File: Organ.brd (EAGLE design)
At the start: 55.5 x 26.7 mm, 16 parts, among them IC1 NE555

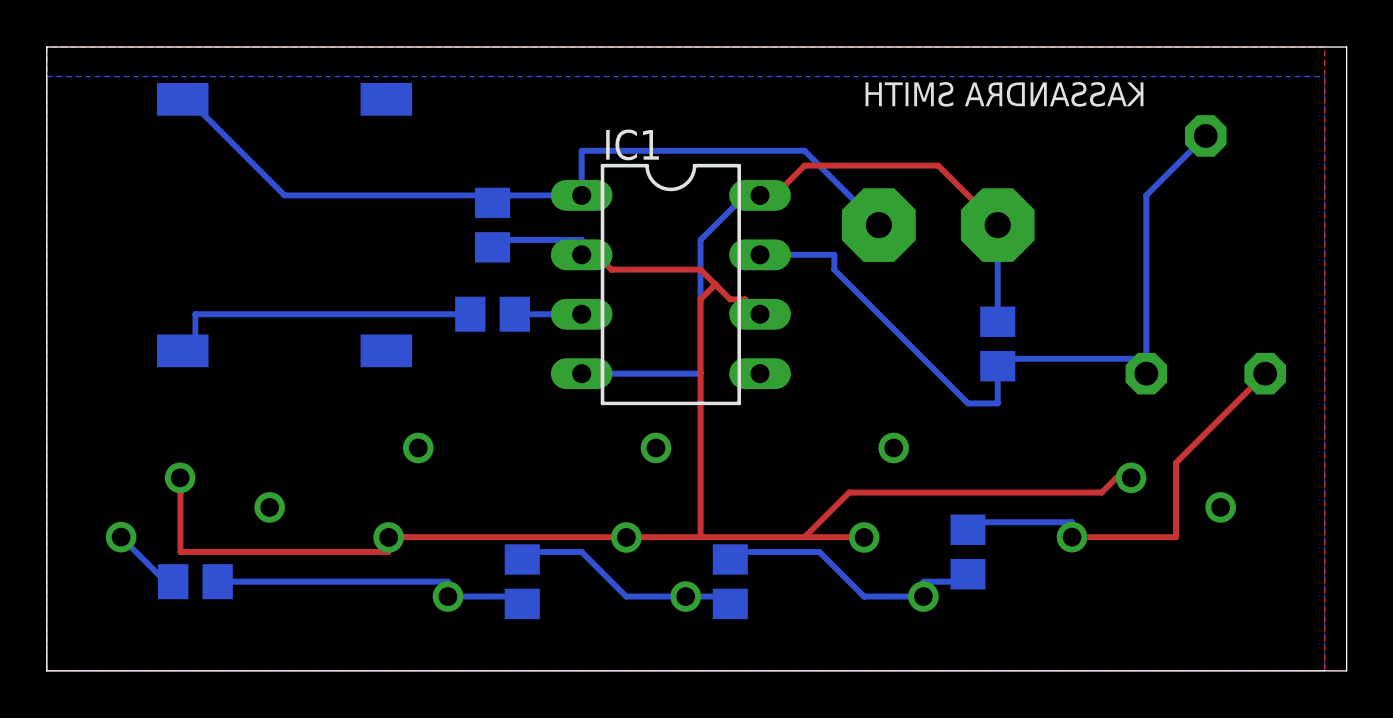
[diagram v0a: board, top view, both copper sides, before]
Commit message: Use new sizing standards
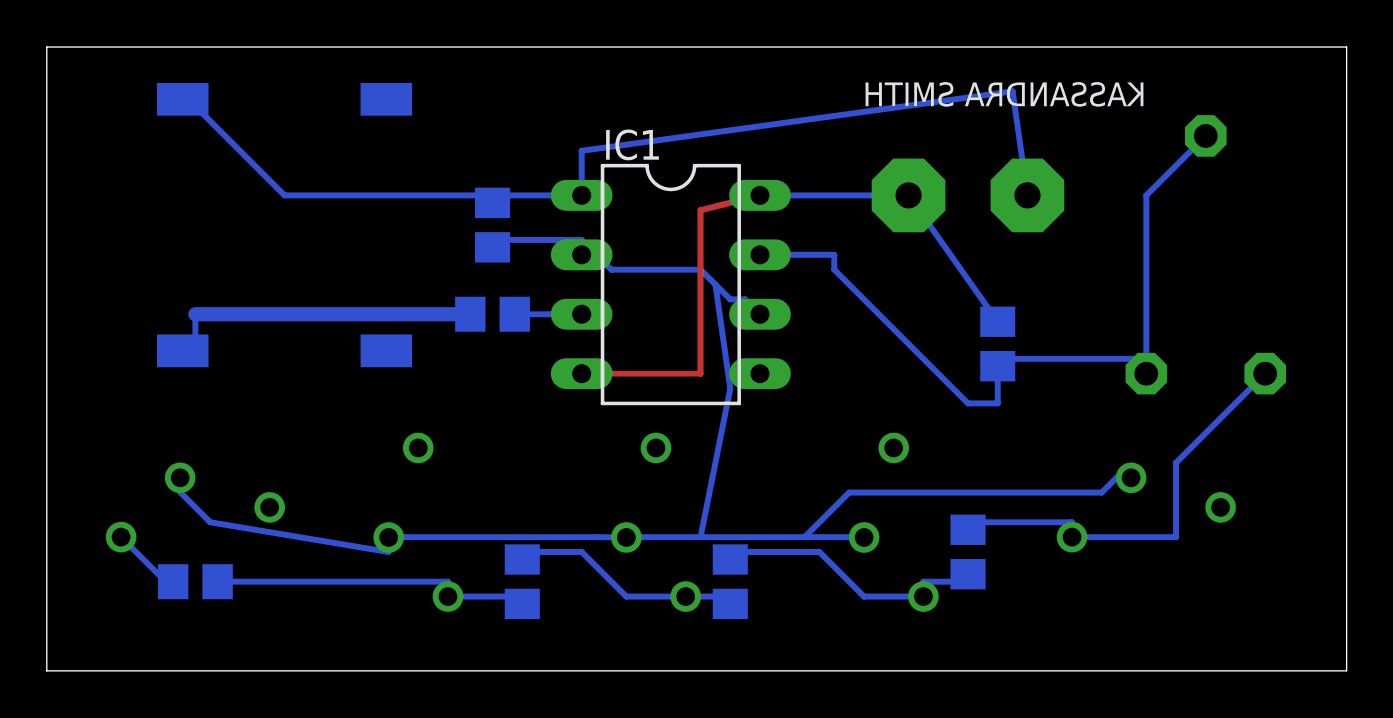
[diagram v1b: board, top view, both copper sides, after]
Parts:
- moved G1 1.80 mm to (39.4, 64.8), turned to 270 degrees
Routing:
- net GROUND: track 34.9 -> 44.0 mm
- net VCC: track 30.0 -> 27.6 mm
- net DISCHARGE: track 72.5 -> 70.5 mm
- removed copper zone on layer 1, net GND
- removed copper zone on layer 16, net GND
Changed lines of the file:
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@@
 <setting verticaltext="up"/>
 </settings>
-<grid distance="0.05" unitdist="inch" unit="inch" style="lines" multiple="1" display="no" altdistance="0.025" altunitdist="inch" altunit="inch"/>
+<grid distance="0.05" unitdist="inch" unit="mm" style="lines" multiple="1" display="no" altdistance="0.025" altunitdist="inch" altunit="mm"/>
 <layers>
 <layer number="1" name="Top" color="4" fill="1" visible="yes" active="yes"/>
@@
 <element name="C1" library="rcl" package="C0805" value="100uF" x="19.05" y="59.69" rot="MR0"/>
 <element name="C2" library="rcl" package="C0805" value="100nF" x="19.05" y="63.5" rot="MR90"/>
-<element name="G1" library="battery" package="AB9V" value="AB9V" x="38.1" y="63.5" rot="MR90"/>
+<element name="G1" library="battery" package="AB9V" value="AB9V" x="39.37" y="64.77" rot="MR270"/>
 <element name="IC1" library="st-microelectronics" package="DIL-08" value="NE555" x="26.67" y="60.96" rot="R270">
 <attribute name="OC_NEWARK" value="89K1486" x="26.67" y="60.96" size="1.778" layer="27" rot="R270" display="off"/>
@@
 <contactref element="R1" pad="2"/>
 <contactref element="IC1" pad="8"/>
-<wire x1="40.64" y1="63.5" x2="40.64" y2="59.37" width="0.254" layer="16"/>
-<wire x1="27.94" y1="57.15" x2="22.86" y2="57.15" width="0.254" layer="16"/>
-<wire x1="27.94" y1="62.865" x2="27.94" y2="57.15" width="0.254" layer="16"/>
-<wire x1="29.845" y1="64.77" x2="27.94" y2="62.865" width="0.254" layer="16"/>
-<wire x1="30.48" y1="64.77" x2="29.845" y2="64.77" width="0.254" layer="16"/>
-<wire x1="38.1" y1="66.04" x2="40.64" y2="63.5" width="0.254" layer="1"/>
-<wire x1="32.385" y1="66.04" x2="38.1" y2="66.04" width="0.254" layer="1"/>
-<wire x1="31.115" y1="64.77" x2="32.385" y2="66.04" width="0.254" layer="1"/>
-<wire x1="30.48" y1="64.77" x2="31.115" y2="64.77" width="0.254" layer="1"/>
+<wire x1="36.83" y1="64.77" x2="40.64" y2="59.37" width="0.254" layer="16"/>
+<wire x1="27.94" y1="57.15" x2="22.86" y2="57.15" width="0.254" layer="1"/>
+<wire x1="27.94" y1="64.135" x2="27.94" y2="57.15" width="0.254" layer="1"/>
+<wire x1="30.48" y1="64.77" x2="27.94" y2="64.135" width="0.254" layer="1"/>
+<wire x1="30.48" y1="64.77" x2="36.83" y2="64.77" width="0.254" layer="16"/>
 </signal>
 <signal name="POT">
@@
 <wire x1="43.815" y1="50.165" x2="43.815" y2="50.8" width="0.254" layer="16"/>
 <wire x1="39.37" y1="50.8" x2="39.37" y2="50.48" width="0.254" layer="16"/>
-<wire x1="48.26" y1="53.34" x2="52.07" y2="57.15" width="0.254" layer="1"/>
-<wire x1="48.26" y1="50.165" x2="48.26" y2="53.34" width="0.254" layer="1"/>
-<wire x1="43.815" y1="50.165" x2="48.26" y2="50.165" width="0.254" layer="1"/>
+<wire x1="48.26" y1="53.34" x2="52.07" y2="57.15" width="0.254" layer="16"/>
+<wire x1="48.26" y1="50.165" x2="48.26" y2="53.34" width="0.254" layer="16"/>
+<wire x1="43.815" y1="50.165" x2="48.26" y2="50.165" width="0.254" layer="16"/>
 </signal>
 <signal name="B4">
@@
 <wire x1="22.86" y1="62.23" x2="22.86" y2="62.865" width="0.254" layer="16"/>
 <wire x1="19.05" y1="62.865" x2="19.05" y2="62.55" width="0.254" layer="16"/>
-<wire x1="29.845" y1="60.325" x2="30.48" y2="59.69" width="0.254" layer="1"/>
-<wire x1="29.21" y1="60.325" x2="29.845" y2="60.325" width="0.254" layer="1"/>
-<wire x1="27.94" y1="61.595" x2="28.575" y2="60.96" width="0.254" layer="1"/>
-<wire x1="28.575" y1="60.96" x2="29.21" y2="60.325" width="0.254" layer="1"/>
-<wire x1="24.13" y1="61.595" x2="27.94" y2="61.595" width="0.254" layer="1"/>
-<wire x1="23.495" y1="62.23" x2="24.13" y2="61.595" width="0.254" layer="1"/>
-<wire x1="22.86" y1="62.23" x2="23.495" y2="62.23" width="0.254" layer="1"/>
-<wire x1="24.765" y1="50.165" x2="15.24" y2="50.165" width="0.254" layer="1"/>
-<wire x1="15.24" y1="50.165" x2="14.61" y2="50.15" width="0.254" layer="1"/>
-<wire x1="24.765" y1="50.165" x2="24.77" y2="50.15" width="0.254" layer="1"/>
-<wire x1="25.4" y1="50.165" x2="27.94" y2="50.165" width="0.254" layer="1"/>
-<wire x1="27.94" y1="50.165" x2="32.385" y2="50.165" width="0.254" layer="1"/>
-<wire x1="32.385" y1="50.165" x2="34.925" y2="50.165" width="0.254" layer="1"/>
-<wire x1="34.925" y1="50.165" x2="34.93" y2="50.15" width="0.254" layer="1"/>
-<wire x1="25.4" y1="50.165" x2="24.77" y2="50.15" width="0.254" layer="1"/>
-<wire x1="5.715" y1="49.53" x2="5.715" y2="52.07" width="0.254" layer="1"/>
-<wire x1="14.605" y1="49.53" x2="5.715" y2="49.53" width="0.254" layer="1"/>
-<wire x1="5.715" y1="52.07" x2="5.7" y2="52.7" width="0.254" layer="1"/>
-<wire x1="14.605" y1="49.53" x2="14.61" y2="50.15" width="0.254" layer="1"/>
-<wire x1="45.085" y1="52.07" x2="45.72" y2="52.705" width="0.254" layer="1"/>
-<wire x1="34.29" y1="52.07" x2="45.085" y2="52.07" width="0.254" layer="1"/>
-<wire x1="32.385" y1="50.165" x2="34.29" y2="52.07" width="0.254" layer="1"/>
-<wire x1="45.72" y1="52.705" x2="46.34" y2="52.7" width="0.254" layer="1"/>
-<wire x1="27.94" y1="60.325" x2="28.575" y2="60.96" width="0.254" layer="1"/>
-<wire x1="27.94" y1="50.165" x2="27.94" y2="60.325" width="0.254" layer="1"/>
+<wire x1="29.845" y1="60.325" x2="30.48" y2="59.69" width="0.254" layer="16"/>
+<wire x1="29.21" y1="60.325" x2="29.845" y2="60.325" width="0.254" layer="16"/>
+<wire x1="27.94" y1="61.595" x2="28.575" y2="60.96" width="0.254" layer="16"/>
+<wire x1="28.575" y1="60.96" x2="29.21" y2="60.325" width="0.254" layer="16"/>
+<wire x1="24.13" y1="61.595" x2="27.94" y2="61.595" width="0.254" layer="16"/>
+<wire x1="23.495" y1="62.23" x2="24.13" y2="61.595" width="0.254" layer="16"/>
+<wire x1="22.86" y1="62.23" x2="23.495" y2="62.23" width="0.254" layer="16"/>
+<wire x1="23.495" y1="50.165" x2="15.24" y2="50.165" width="0.254" layer="16"/>
+<wire x1="15.24" y1="50.165" x2="14.61" y2="50.15" width="0.254" layer="16"/>
+<wire x1="23.495" y1="50.165" x2="24.77" y2="50.15" width="0.254" layer="16"/>
+<wire x1="25.4" y1="50.165" x2="27.94" y2="50.165" width="0.254" layer="16"/>
+<wire x1="27.94" y1="50.165" x2="32.385" y2="50.165" width="0.254" layer="16"/>
+<wire x1="32.385" y1="50.165" x2="34.925" y2="50.165" width="0.254" layer="16"/>
+<wire x1="34.925" y1="50.165" x2="34.93" y2="50.15" width="0.254" layer="16"/>
+<wire x1="25.4" y1="50.165" x2="24.77" y2="50.15" width="0.254" layer="16"/>
+<wire x1="6.985" y1="50.8" x2="5.715" y2="52.07" width="0.254" layer="16"/>
+<wire x1="14.605" y1="49.53" x2="6.985" y2="50.8" width="0.254" layer="16"/>
+<wire x1="5.715" y1="52.07" x2="5.7" y2="52.7" width="0.254" layer="16"/>
+<wire x1="14.605" y1="49.53" x2="14.61" y2="50.15" width="0.254" layer="16"/>
+<wire x1="45.085" y1="52.07" x2="45.72" y2="52.705" width="0.254" layer="16"/>
+<wire x1="34.29" y1="52.07" x2="45.085" y2="52.07" width="0.254" layer="16"/>
+<wire x1="32.385" y1="50.165" x2="34.29" y2="52.07" width="0.254" layer="16"/>
+<wire x1="45.72" y1="52.705" x2="46.34" y2="52.7" width="0.254" layer="16"/>
+<wire x1="29.21" y1="56.515" x2="28.575" y2="60.96" width="0.254" layer="16"/>
+<wire x1="27.94" y1="50.165" x2="29.21" y2="56.515" width="0.254" layer="16"/>
 </signal>
 <signal name="GROUND">
@@
 <wire x1="6.35" y1="68.58" x2="5.81" y2="68.875" width="0.254" layer="16"/>
 <wire x1="19.05" y1="64.77" x2="19.05" y2="64.45" width="0.254" layer="16"/>
-<wire x1="32.385" y1="66.675" x2="35.56" y2="63.5" width="0.254" layer="16"/>
-<wire x1="22.86" y1="66.675" x2="32.385" y2="66.675" width="0.254" layer="16"/>
+<wire x1="41.275" y1="69.215" x2="41.91" y2="64.77" width="0.254" layer="16"/>
+<wire x1="22.86" y1="66.675" x2="41.275" y2="69.215" width="0.254" layer="16"/>
 <wire x1="22.86" y1="64.77" x2="22.86" y2="66.675" width="0.254" layer="16"/>
 </signal>
@@
 <contactref element="C1" pad="2"/>
 <contactref element="SP1" pad="+"/>
-<wire x1="6.35" y1="59.69" x2="18.1" y2="59.69" width="0.254" layer="16"/>
+<wire x1="6.35" y1="59.69" x2="18.1" y2="59.69" width="0.6096" layer="16"/>
 <wire x1="6.35" y1="58.42" x2="6.35" y2="59.69" width="0.254" layer="16"/>
 <wire x1="6.35" y1="58.42" x2="5.81" y2="58.125" width="0.254" layer="16"/>
 </signal>
-<signal name="GND">
-<polygon width="0.4064" layer="16">
-<vertex x="0" y="69.85"/>
-<vertex x="54.61" y="69.85"/>
-<vertex x="54.61" y="44.45"/>
-<vertex x="0" y="44.45"/>
-</polygon>
-<polygon width="0.4064" layer="1">
-<vertex x="0" y="71.12"/>
-<vertex x="0" y="44.45"/>
-<vertex x="54.61" y="44.45"/>
-<vertex x="54.61" y="71.12"/>
-</polygon>
-</signal>
 </signals>
